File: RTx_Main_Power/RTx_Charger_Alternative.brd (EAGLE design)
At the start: 9 parts, among them IC1 TL331, Q1 STW11NM80

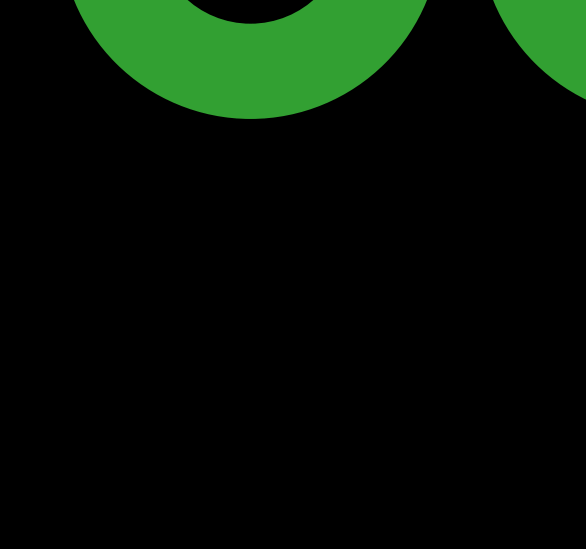
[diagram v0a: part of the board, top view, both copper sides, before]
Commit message: Added voltage divider to inverting input of opamp.
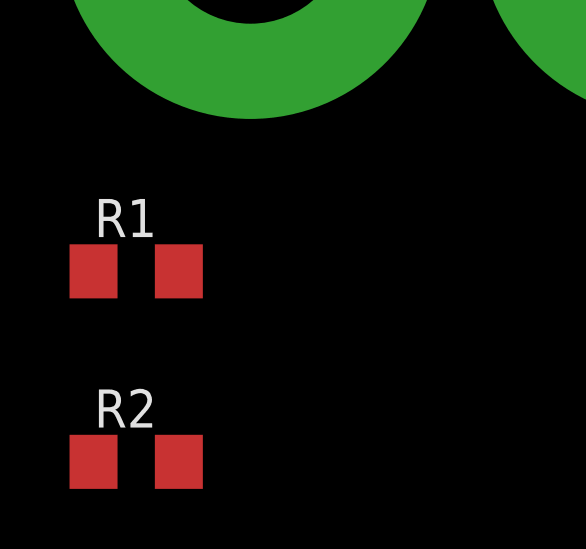
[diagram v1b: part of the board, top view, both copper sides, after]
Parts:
- added R1: 10k, motorFeedback:R1206
- added R2: 230k, motorFeedback:R1206
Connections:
- new net N$7: R1.2, U$2.P$1
- net GND: now also R2.2
- net N$6: now also R1.1, R2.1; no longer U$2.P$1
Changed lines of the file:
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@@
 <element name="U$5" library="temp_library" package="TERMINAL_RELAY" value="TERMINAL" x="-283.21" y="-139.7"/>
 <element name="U$7" library="temp_library" package="TERMINAL_RELAY" value="TERMINAL" x="-297.18" y="-139.7"/>
+<element name="R1" library="motorFeedback" package="R1206" value="10k" x="-300.99" y="-151.13"/>
+<element name="R2" library="motorFeedback" package="R1206" value="230k" x="-300.99" y="-157.48"/>
 </elements>
 <signals>
@@
 <signal name="N$6">
 <contactref element="IC1" pad="1"/>
-<contactref element="U$2" pad="P$1"/>
-<wire x1="-16.19" y1="-47.026" x2="-241.3" y2="-139.7" width="0" layer="19" extent="1-1"/>
+<contactref element="R1" pad="1"/>
+<contactref element="R2" pad="1"/>
+<wire x1="-302.412" y1="-151.13" x2="-302.412" y2="-157.48" width="0" layer="19" extent="1-1"/>
+<wire x1="-16.19" y1="-47.026" x2="-302.412" y2="-151.13" width="0" layer="19" extent="1-1"/>
 </signal>
 <signal name="GND">
@@
 <contactref element="U$6" pad="2"/>
 <contactref element="U$3" pad="P$1"/>
+<contactref element="R2" pad="2"/>
+<wire x1="-255.27" y1="-139.7" x2="-299.568" y2="-157.48" width="0" layer="19" extent="1-1"/>
 <wire x1="-222.25" y1="-140.462" x2="-255.27" y2="-139.7" width="0" layer="19" extent="1-1"/>
 <wire x1="-155.829" y1="-121.92" x2="-222.25" y2="-140.462" width="0" layer="19" extent="1-1"/>
 <wire x1="-15.24" y1="-47.026" x2="-155.829" y2="-121.92" width="0" layer="19" extent="1-1"/>
 </signal>
+<signal name="N$7">
+<contactref element="U$2" pad="P$1"/>
+<contactref element="R1" pad="2"/>
+<wire x1="-241.3" y1="-139.7" x2="-299.568" y2="-151.13" width="0" layer="19" extent="1-1"/>
+</signal>
 </signals>

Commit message: Updated controller schematic with high speed signal routing information. Added termination resistor to SPI_SCK line. Included Sightline documentation. Added avionics library, node4-2.lbr, to RTx controller library folder. Made progress on RTx_Charger board layout.
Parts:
- U$2, U$3, U$4, U$5, U$7: device temp_library:TERMINAL_RELAY -> temp_library:TERMINAL_BATTERY
- moved R2 405.6 mm to (58.4, 30.5), turned to 90 degrees
- moved R1 398.2 mm to (52.1, 33.0), turned to 90 degrees
- moved U$3 381.2 mm to (90.2, 21.6)
- moved U$2 378.0 mm to (90.2, 41.9)
- moved U$4 375.5 mm to (69.8, 21.6)
- moved U$7 348.2 mm to (11.4, 21.6)
- moved U$5 346.1 mm to (11.4, 41.9)
- moved U$6 304.6 mm to (45.7, 8.89), turned to 180 degrees
- moved Q1 258.6 mm to (38.7, 41.9)
- moved R3 246.4 mm to (38.7, 24.1), turned to 270 degrees
- moved IC1 95.7 mm to (50.2, 24.1), turned to 180 degrees
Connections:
- removed net N$2: IC1.5, U$4.P$1, U$6.1
- removed net N$3: U$6.3, U$7.P$1
- removed net N$4: Q1.1, U$5.P$1
- removed net N$7: R1.2, U$2.P$1
- new net RELAY1: IC1.3, U$6.3, U$7.1
- new net RELAY2: Q1.1, U$5.1
- new net VCC1: R1.2, U$2.1
- new net VCC2: IC1.5, U$4.1, U$6.1
- net GND: now also U$3.1; no longer U$3.P$1
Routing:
- net RELAY1: track 0.00 -> 71.6 mm, vias 0 -> 2
- net VCC1: track 0.00 -> 44.1 mm
- net VCC2: track 0.00 -> 28.6 mm
- net RELAY2: track 0.00 -> 21.8 mm
- net N$5: track 0.00 -> 16.4 mm
- net N$6: track 0.00 -> 15.4 mm
- net N$1: track 0.00 -> 14.4 mm
- added copper zone on layer 1, net GND
- added copper zone on layer 16, net GND
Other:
- board outline added: 133.4 x 95.2 mm
